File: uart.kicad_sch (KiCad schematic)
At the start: 42 parts, among them J3 USB_C_Receptacle, U12 TPD4E02B04DQA, U3 CP2104, U4 AIP74LVC1T45GB236TR

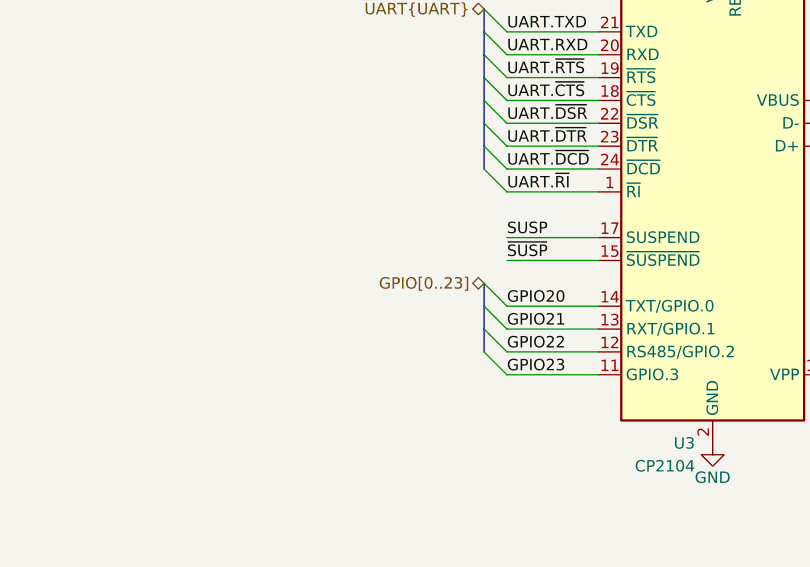
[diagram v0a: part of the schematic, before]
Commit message: *.kicad_sch: expand gpio to [0..31]
Signed-off-by: Huang Rui <vowstar@gmail.com>
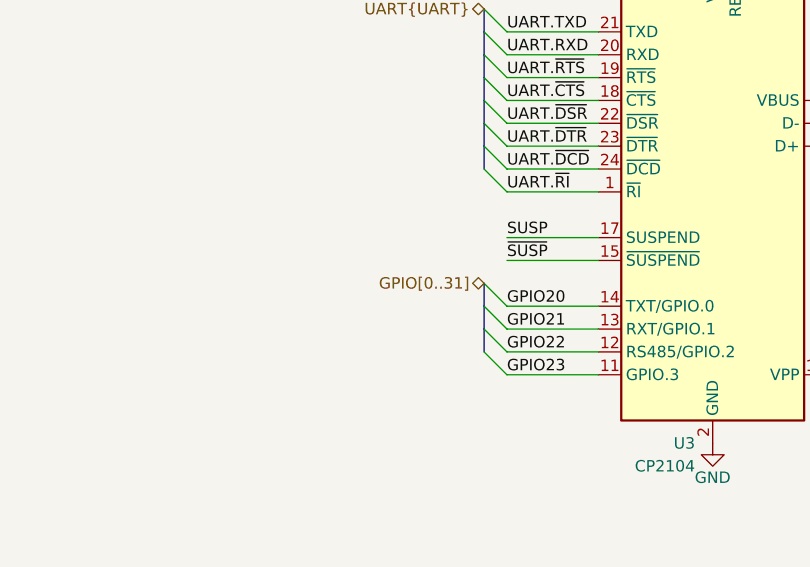
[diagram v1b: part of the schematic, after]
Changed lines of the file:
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@@
     (comment 4 "Rui Huang (2023-03-02)")
   )
+  (bus_alias "UART" (members "TXD" "RXD" "~{RTS}" "~{CTS}" "~{DSR}" "~{DTR}" "~{DCD}" "~{RI}"))
   (bus_alias "SDIO" (members "DAT0" "DAT1" "DAT2" "DAT3" "CMD" "CLK"))
-  (bus_alias "UART" (members "TXD" "RXD" "~{RTS}" "~{CTS}" "~{DSR}" "~{DTR}" "~{DCD}" "~{RI}"))
   (junction (at 173.99 24.13) (diameter 0) (color 0 0 0 0)
   )
@@
     (effects (font (size 1.27 1.27)) (justify right))
   )
-  (hierarchical_label "GPIO[0..23]" (shape tri_state) (at 148.59 74.93 180) (fields_autoplaced)
+  (hierarchical_label "GPIO[0..31]" (shape tri_state) (at 148.59 74.93 180) (fields_autoplaced)
     (effects (font (size 1.27 1.27)) (justify right))
   )

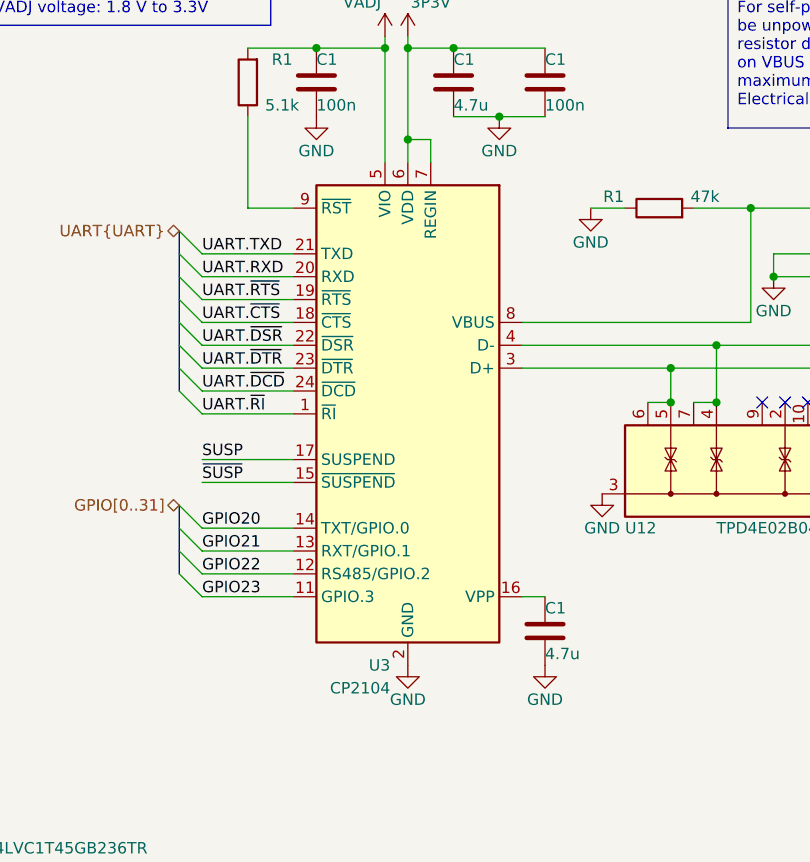
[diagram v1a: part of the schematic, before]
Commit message: *.kicad_sch: add more detailed annotations for signals
Signed-off-by: Huang Rui <vowstar@gmail.com>
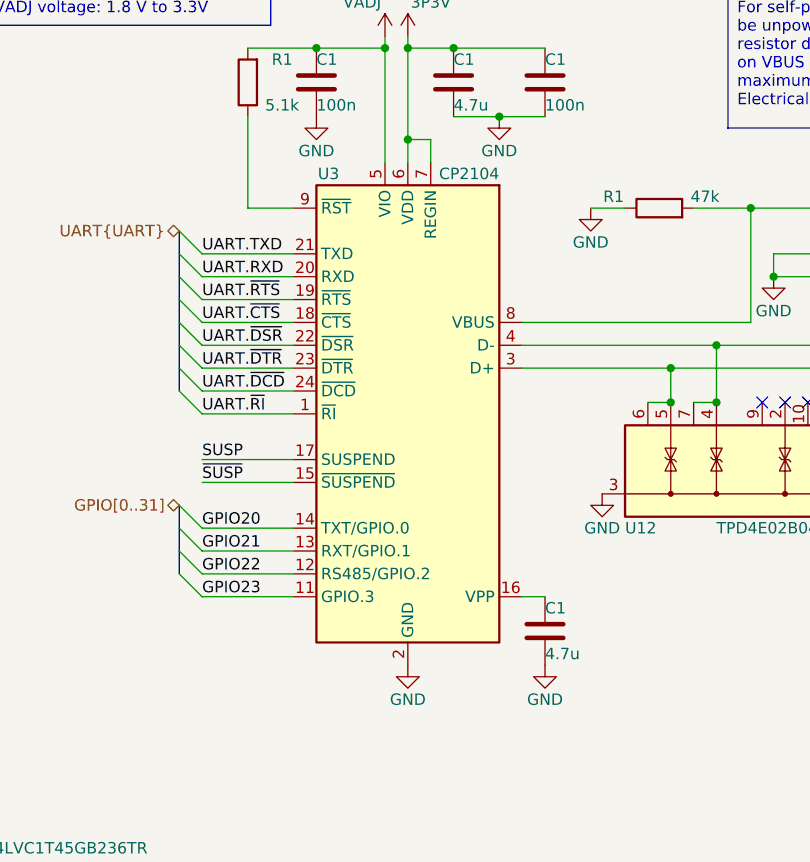
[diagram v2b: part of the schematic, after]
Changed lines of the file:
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@@
     (comment 4 "Rui Huang (2023-03-02)")
   )
-  (bus_alias "UART" (members "TXD" "RXD" "~{RTS}" "~{CTS}" "~{DSR}" "~{DTR}" "~{DCD}" "~{RI}"))
   (bus_alias "SDIO" (members "DAT0" "DAT1" "DAT2" "DAT3" "CMD" "CLK"))
+  (bus_alias "UART" (members "TXD" "RXD" "~{RTS}" "~{CTS}" "~{DSR}" "~{DTR}" "~{DCD}" "~{RI}"))
   (junction (at 173.99 24.13) (diameter 0) (color 0 0 0 0)
   )
@@
   (symbol (lib_id "CHIPSAlliance_Interface:CP2104") (at 184.15 39.37 0) (mirror y) (unit 1)
     (in_bom yes) (on_board yes) (dnp no)
-    (property "Reference" "U3" (at 172.0341 92.71 0)
+    (property "Reference" "U3" (at 166.37 38.1 0)
       (effects (font (size 1.27 1.27)) (justify left))
     )
-    (property "Value" "CP2104" (at 172.0341 95.25 0)
+    (property "Value" "CP2104" (at 184.15 38.1 0)
       (effects (font (size 1.27 1.27)) (justify left))
     )

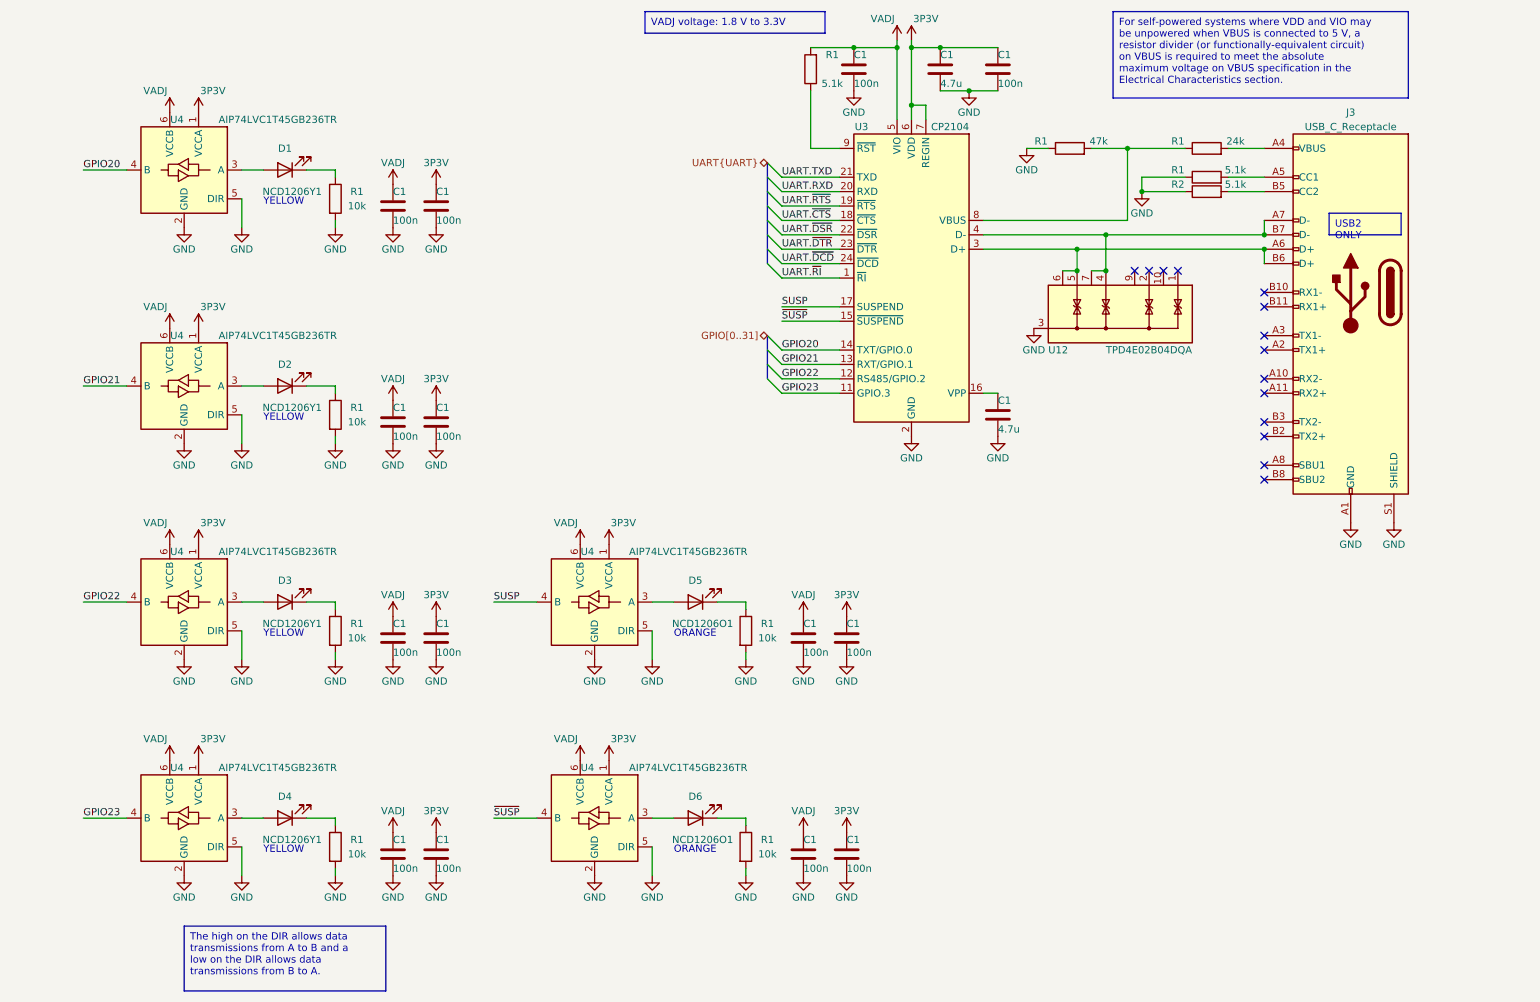
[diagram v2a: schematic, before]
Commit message: *.kicad_sch: adjust schematic symbol coordinates
Signed-off-by: Huang Rui <vowstar@gmail.com>
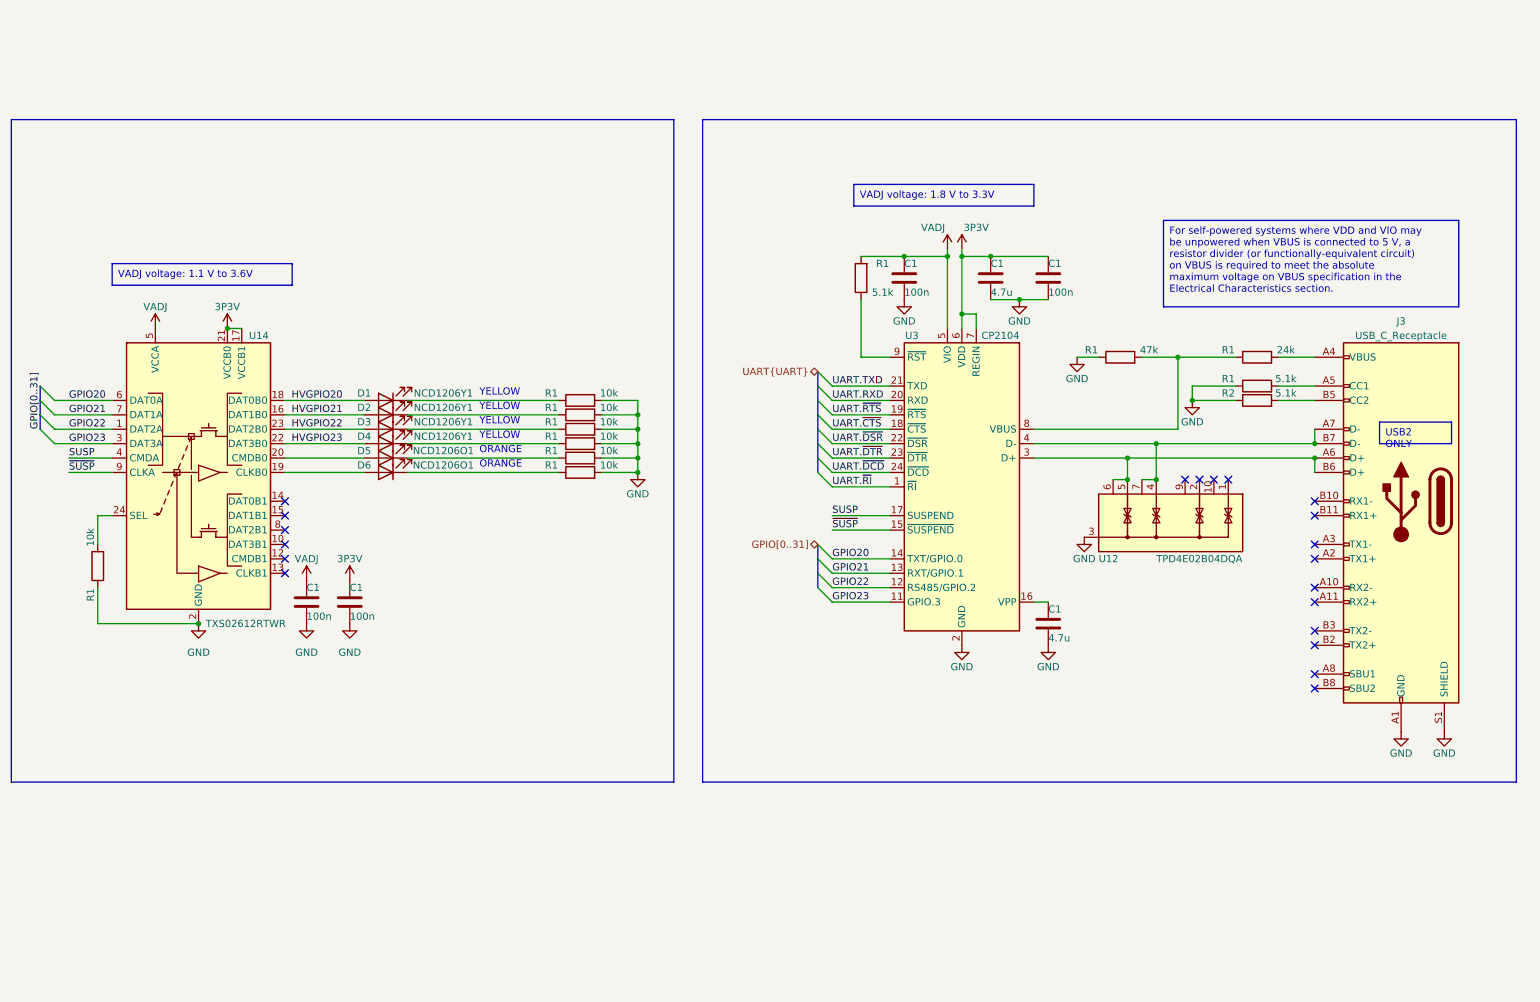
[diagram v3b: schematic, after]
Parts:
- removed C1 (x12): 100n, Capacitor_SMD:C_0402_1005Metric, symbol Device:C
- removed U4 (x6): AIP74LVC1T45GB236TR, Package_TO_SOT_SMD:SOT-23-6, symbol CHIPSAlliance_Logic:AIP74LVC1T45GB236TR
- added C1 (x2): 100n, Capacitor_SMD:C_0402_1005Metric, symbol Device:C
- added R1: 10k, Resistor_SMD:R_0402_1005Metric, symbol Device:R
- added U14: TXS02612RTWR, Package_DFN_QFN:WQFN-24-1EP_4x4mm_P0.5mm_EP2.45x2.45mm, symbol CHIPSAlliance_Logic:TXS02612RTWR
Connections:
- net 3P3V: now also C1.1, U14.17 (VCCB1), U14.21 (VCCB0)
- net GND: now also C1.2, C1.2, R1.1, U14.11 (GND), U14.2 (GND), U14.25 (GND)
- net GPIO20: now also U14.6 (DAT0A)
- net GPIO21: now also U14.7 (DAT1A)
- net GPIO22: now also U14.1 (DAT2A)
- net GPIO23: now also U14.3 (DAT3A)
- net SUSP: now also U14.4 (CMDA)
- net VADJ: now also C1.1, U14.5 (VCCA)
- net ~{SUSP}: now also U14.9 (CLKA)
- net HVGPIO20: now reaches D1.2 (A)
- net HVGPIO20: now also U14.18 (DAT0B0)
- net HVGPIO21: now reaches D2.2 (A)
- net HVGPIO21: now also U14.16 (DAT1B0)
- net HVGPIO23: now reaches D4.2 (A)
- net HVGPIO23: now also U14.22 (DAT3B0)
- net at D5.2 (A): now also U14.20 (CMDB0)
- net at D6.2 (A): now also U14.19 (CLKB0)
- net HVGPIO22: now reaches D3.2 (A)
- net HVGPIO22: now also U14.23 (DAT2B0)
- new net: R1.2, U14.24 (SEL)
- no-connect marks 14 -> 20
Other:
- moved on the sheet: C1, D1, D2, D3, D4, D5, D6, J3, R1, R2, U12, U3

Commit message: *.kicad_sch: update symbol to fix footprint 3d model
- fix TXS02612RTWR 3d model
- fix micro-sd socket 3d model

Signed-off-by: Huang Rui <vowstar@gmail.com>
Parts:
- U14: footprint Package_DFN_QFN:WQFN-24-1EP_4x4mm_P0.5mm_EP2.45x2.45mm -> CHIPSAlliance_Logic:WQFN-24-1EP_4x4mm_P0.5mm_EP2.45x2.45mm
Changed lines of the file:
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@@
     (comment 4 "Rui Huang (2023-03-02)")
   )
+  (bus_alias "UART" (members "TXD" "RXD" "~{RTS}" "~{CTS}" "~{DSR}" "~{DTR}" "~{DCD}" "~{RI}"))
   (bus_alias "SDIO" (members "DAT0" "DAT1" "DAT2" "DAT3" "CMD" "CLK"))
-  (bus_alias "UART" (members "TXD" "RXD" "~{RTS}" "~{CTS}" "~{DSR}" "~{DTR}" "~{DCD}" "~{RI}"))
   (junction (at 182.88 60.96) (diameter 0) (color 0 0 0 0)
   )
@@
       (effects (font (size 1.27 1.27)) (justify left))
     )
-    (property "Footprint" "Package_DFN_QFN:WQFN-24-1EP_4x4mm_P0.5mm_EP2.45x2.45mm" (at 35.56 127 0)
+    (property "Footprint" "CHIPSAlliance_Logic:WQFN-24-1EP_4x4mm_P0.5mm_EP2.45x2.45mm" (at 35.56 127 0)
       (effects (font (size 1.27 1.27)) (justify left) hide)
     )
